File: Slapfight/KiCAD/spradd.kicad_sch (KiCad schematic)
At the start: 20 parts

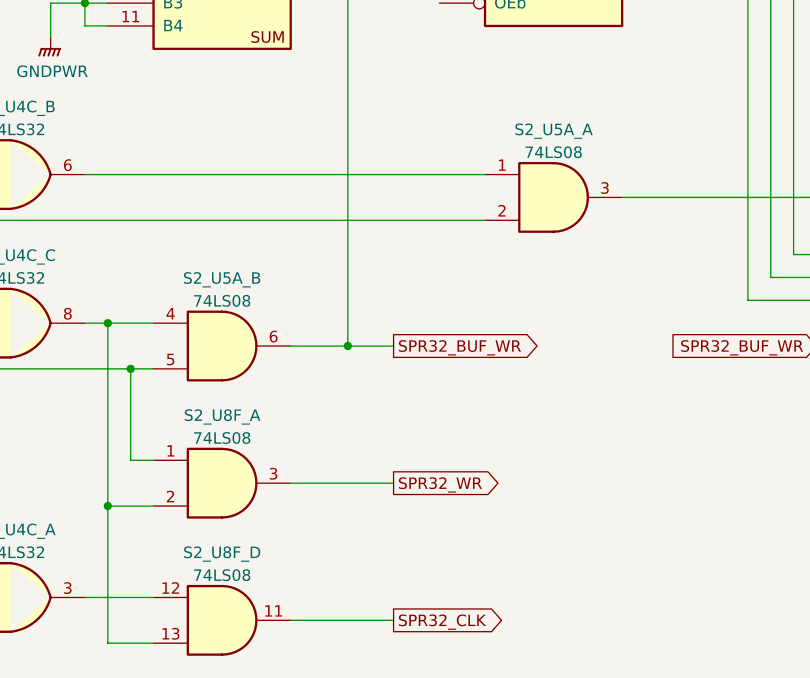
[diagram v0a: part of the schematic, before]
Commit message: Component naming updates
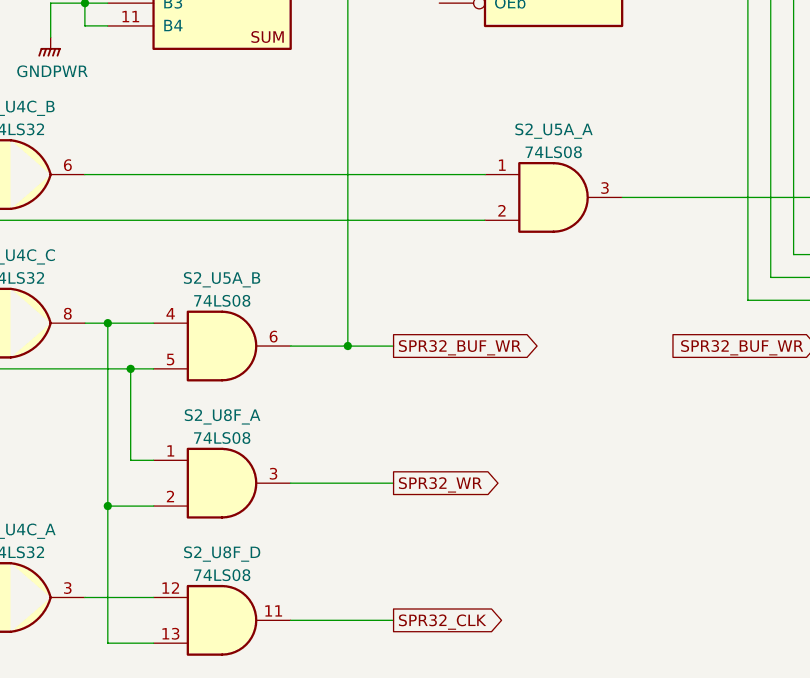
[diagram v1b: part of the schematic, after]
